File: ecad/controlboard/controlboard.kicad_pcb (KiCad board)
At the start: 2 copper layers, 50 x 100 mm, 39 parts, among them J1 B6B-XH-A(LF)(SN), SW1 KSC_SLT_241G_LFS

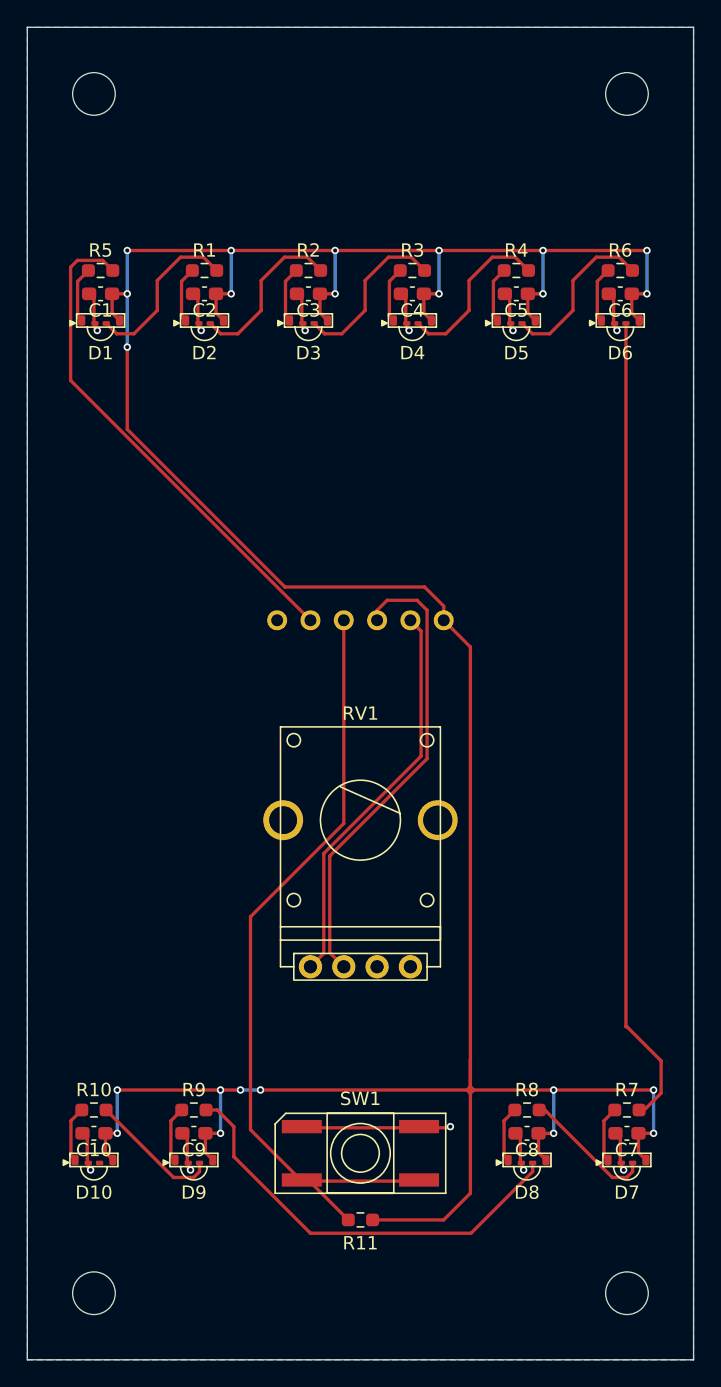
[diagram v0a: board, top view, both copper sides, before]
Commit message: Small changes and cleanup as 3dmodels are pieced together.
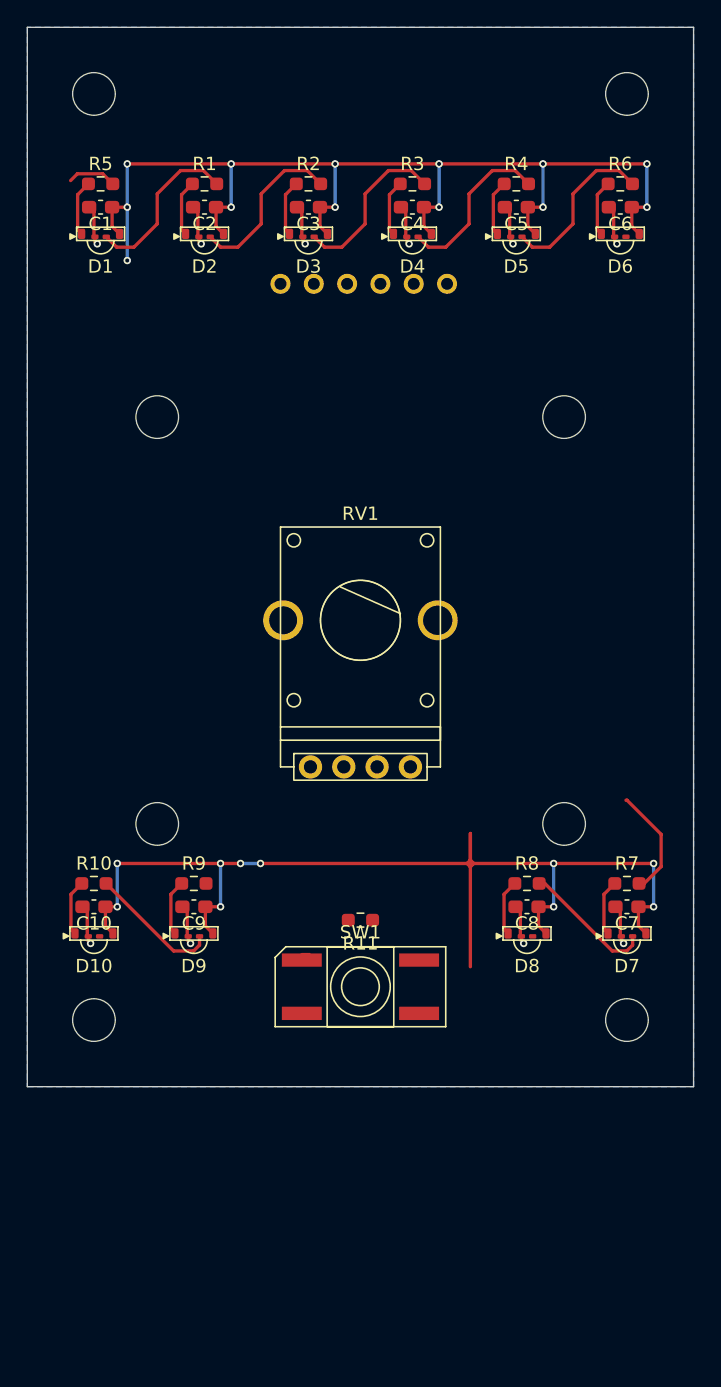
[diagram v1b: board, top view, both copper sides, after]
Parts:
- added REF**: MountingHole_3.2mm_M3, MountingHole:MountingHole_3.2mm_M3, F.Cu at (132.2, 79.8)
- added REF**4: MountingHole_3.2mm_M3, MountingHole:MountingHole_3.2mm_M3, F.Cu at (162.8, 79.8)
- added REF**5: MountingHole_3.2mm_M3, MountingHole:MountingHole_3.2mm_M3, F.Cu at (132.2, 110.3)
- added REF**6: MountingHole_3.2mm_M3, MountingHole:MountingHole_3.2mm_M3, F.Cu at (162.8, 110.3)
- moved J1 25.3 mm to (147.8, 69.8)
- moved R11 22.5 mm to (147.5, 117.5)
- moved REF**2 20.5 mm to (127.5, 125.0)
- moved REF**3 20.5 mm to (167.5, 125.0)
- moved C10 17.0 mm to (127.5, 116.5)
- moved C7 17.0 mm to (167.5, 116.5)
- moved C8 17.0 mm to (160.0, 116.5)
- moved C9 17.0 mm to (135.0, 116.5)
- moved D10 17.0 mm to (127.5, 118.5)
- moved D7 17.0 mm to (167.5, 118.5)
- moved D8 17.0 mm to (160.0, 118.5)
- moved D9 17.0 mm to (135.0, 118.5)
- moved R10 17.0 mm to (127.5, 114.8)
- moved R7 17.0 mm to (167.5, 114.8)
- moved R8 17.0 mm to (160.0, 114.8)
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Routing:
- net +5V: track 240.3 -> 161.9 mm
- net Net-(J1-Pad3): track 60.1 -> 0.00 mm
- net Net-(D6-DOut): track 61.1 -> 8.30 mm
- net Net-(J1-Pad4): track 35.3 -> 0.00 mm
- net Net-(J1-Pad2): track 37.6 -> 3.69 mm
- net Net-(D8-DOut): track 32.2 -> 0.00 mm
- net Net-(J1-Pad5): track 29.8 -> 0.00 mm
- net GND: track 41.2 -> 30.6 mm, vias 11 -> 10
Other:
- board size 50 x 100 mm -> 50 x 79.5 mm

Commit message: Change addressable LED to new part that is still available.
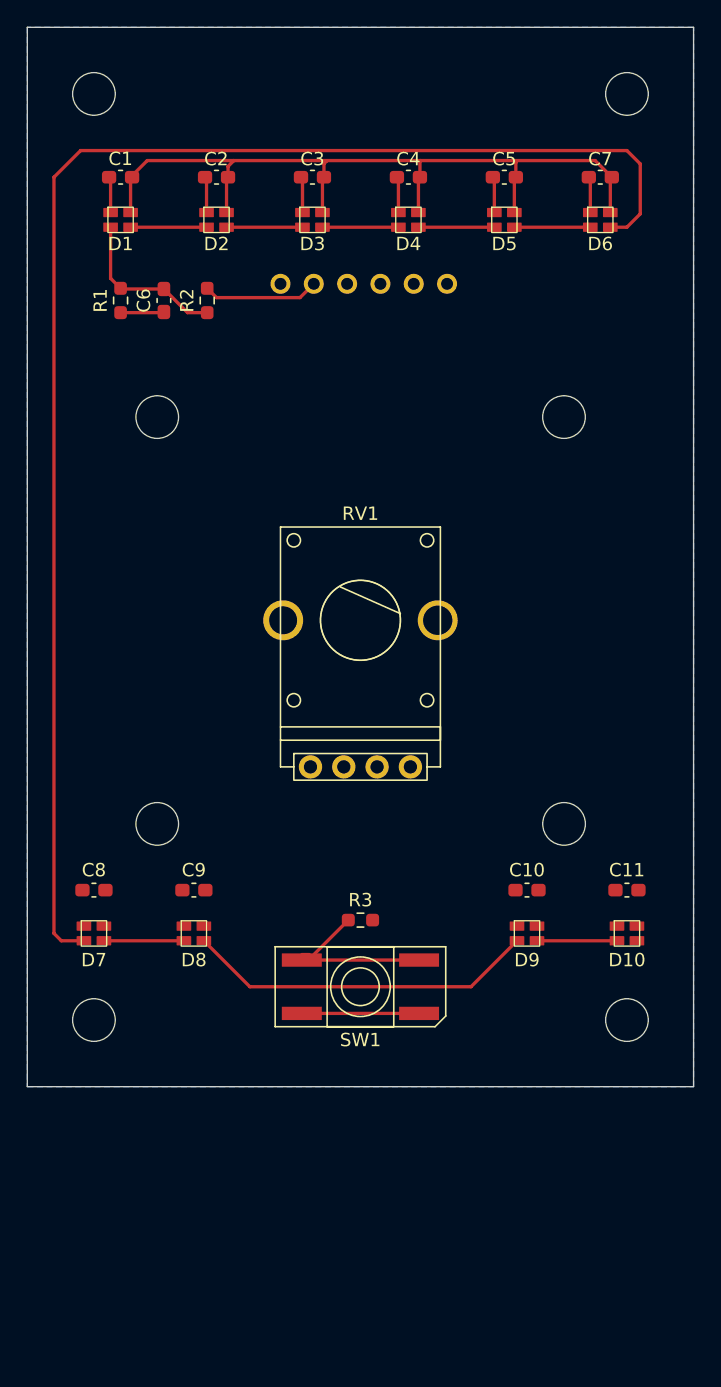
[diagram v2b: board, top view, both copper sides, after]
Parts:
- removed the R1 at (135.8, 62.2)
- removed R10, R4, R6, R7, R8, R9: 33, Resistor_SMD:R_0603_1608Metric_Pad0.98x0.95mm_HandSolder
- removed the R3 at (151.4, 62.2)
- removed REF**1, REF**2, REF**3, REF**4, REF**5, REF**6: MountingHole_3.2mm_M3, MountingHole:MountingHole_3.2mm_M3
- removed control_plate: Board, PCM_kikit:Board
- added C6: 0.1u, Capacitor_SMD:C_0603_1608Metric_Pad1.08x0.95mm_HandSolder, F.Cu at (132.8, 71.0)
- added REF**: MountingHole_3.2mm_M3, MountingHole:MountingHole_3.2mm_M3, F.Cu at (162.8, 110.3)
- added REF**: MountingHole_3.2mm_M3, MountingHole:MountingHole_3.2mm_M3, F.Cu at (167.5, 55.5)
- added REF**: MountingHole_3.2mm_M3, MountingHole:MountingHole_3.2mm_M3, F.Cu at (162.8, 79.8)
- added REF**: MountingHole_3.2mm_M3, MountingHole:MountingHole_3.2mm_M3, F.Cu at (167.5, 125.0)
- added REF**: MountingHole_3.2mm_M3, MountingHole:MountingHole_3.2mm_M3, F.Cu at (132.2, 110.3)
- added REF**: MountingHole_3.2mm_M3, MountingHole:MountingHole_3.2mm_M3, F.Cu at (127.5, 125.0)
- D1, D10, D2, D3, D4, D5, D6, D7, D8, D9: value 12-23C/RSGHBHW-5V01/2C -> 19-C47/RSGHBHC-5V01/2T; footprint silver-box-feetprints:12-23C-RSGHBHW-5V01-2C -> silver-box-feetprints:19-C47 RSGHBHC-5V01 2T
- R1: renamed from R5; value 33 -> 100k
- R2: value 33 -> 10
- moved C11 40.0 mm to (167.5, 115.2)
- moved C8 40.0 mm to (127.5, 115.2)
- moved D10 40.0 mm to (167.5, 118.5)
- moved D7 40.0 mm to (127.5, 118.5)
- moved C10 25.0 mm to (160.0, 115.2)
- moved C9 25.0 mm to (135.0, 115.2)
- moved D8 25.0 mm to (135.0, 118.5)
- moved D9 25.0 mm to (160.0, 118.5)
- moved R2 11.6 mm to (136.0, 71.0), turned to 90 degrees
- moved R1 8.88 mm to (129.5, 71.0), turned to 90 degrees
- moved C1 2.70 mm to (129.5, 61.8)
- moved C7 2.70 mm to (165.5, 61.8)
- moved C2 2.42 mm to (136.7, 61.8)
- moved C5 2.42 mm to (158.3, 61.8)
- moved C3 2.27 mm to (143.9, 61.8)
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- renumbered C9 to C10, C10 to C11, C6 to C7, C7 to C8, C8 to C9, R11 to R3
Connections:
- D1 pad 1: Net-(D1-DIn) -> Net-(D1-DOut)
- D1 pad 2: GND -> +5V
- D1 pad 3: Net-(D1-DOut) -> Net-(D1-DIn)
- D1 pad 4: +5V -> GND
- D10 pad 1: Net-(D10-DIn) -> unconnected-(D10-DOut-Pad1)
- D10 pad 2: GND -> +5V
- D10 pad 3: unconnected-(D10-DOut-Pad3) -> Net-(D10-DIn)
- D10 pad 4: +5V -> GND
- D2 pad 1: Net-(D2-DIn) -> Net-(D2-DOut)
- D2 pad 2: GND -> +5V
- D2 pad 3: Net-(D2-DOut) -> Net-(D1-DOut)
- D2 pad 4: +5V -> GND
- D3 pad 1: Net-(D3-DIn) -> Net-(D3-DOut)
- D3 pad 2: GND -> +5V
- D3 pad 3: Net-(D3-DOut) -> Net-(D2-DOut)
- D3 pad 4: +5V -> GND
- D4 pad 1: Net-(D4-DIn) -> Net-(D4-DOut)
- D4 pad 2: GND -> +5V
- D4 pad 3: Net-(D4-DOut) -> Net-(D3-DOut)
- D4 pad 4: +5V -> GND
- D5 pad 1: Net-(D5-DIn) -> Net-(D5-DOut)
- D5 pad 2: GND -> +5V
- D5 pad 3: Net-(D5-DOut) -> Net-(D4-DOut)
- D5 pad 4: +5V -> GND
- D6 pad 1: Net-(D6-DIn) -> Net-(D6-DOut)
- D6 pad 2: GND -> +5V
- D6 pad 3: Net-(D6-DOut) -> Net-(D5-DOut)
- D6 pad 4: +5V -> GND
- D7 pad 1: Net-(D7-DIn) -> Net-(D7-DOut)
- D7 pad 2: GND -> +5V
- D7 pad 3: Net-(D7-DOut) -> Net-(D6-DOut)
- D7 pad 4: +5V -> GND
- D8 pad 1: Net-(D8-DIn) -> Net-(D8-DOut)
- D8 pad 2: GND -> +5V
- D8 pad 3: Net-(D8-DOut) -> Net-(D7-DOut)
- D8 pad 4: +5V -> GND
- D9 pad 1: Net-(D9-DIn) -> Net-(D10-DIn)
- D9 pad 2: GND -> +5V
- D9 pad 3: Net-(D9-DOut) -> Net-(D8-DOut)
- D9 pad 4: +5V -> GND
- R1 pad 1: Net-(D1-DIn) -> GND
- R1 pad 2: Net-(J1-Pad2) -> Net-(D1-DIn)
- R2 pad 1: Net-(D3-DIn) -> Net-(D1-DIn)
- R2 pad 2: Net-(D2-DOut) -> Net-(J1-Pad2)
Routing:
- net +5V: track 161.9 -> 58.6 mm, vias 23 -> 0
- net Net-(D6-DOut): track 8.30 -> 110.9 mm
- net Net-(D8-DOut): track 0.00 -> 26.4 mm
- net Net-(J1-Pad3): track 0.00 -> 14.1 mm
- net Net-(D9-DOut): track 9.95 -> 0.00 mm
- net Net-(D1-DIn): track 4.21 -> 12.2 mm
- net Net-(D3-DOut): track 12.7 -> 5.70 mm
- net Net-(D5-DOut): track 12.7 -> 5.70 mm
- net Net-(D4-DOut): track 12.7 -> 5.70 mm
- net Net-(D1-DOut): track 12.7 -> 5.70 mm
- net Net-(D2-DOut): track 12.7 -> 5.70 mm
- net Net-(J1-Pad2): track 3.69 -> 8.72 mm
- net Net-(D5-DIn): track 4.21 -> 0.00 mm
- net Net-(D3-DIn): track 4.21 -> 0.00 mm
- net Net-(D2-DIn): track 4.21 -> 0.00 mm
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
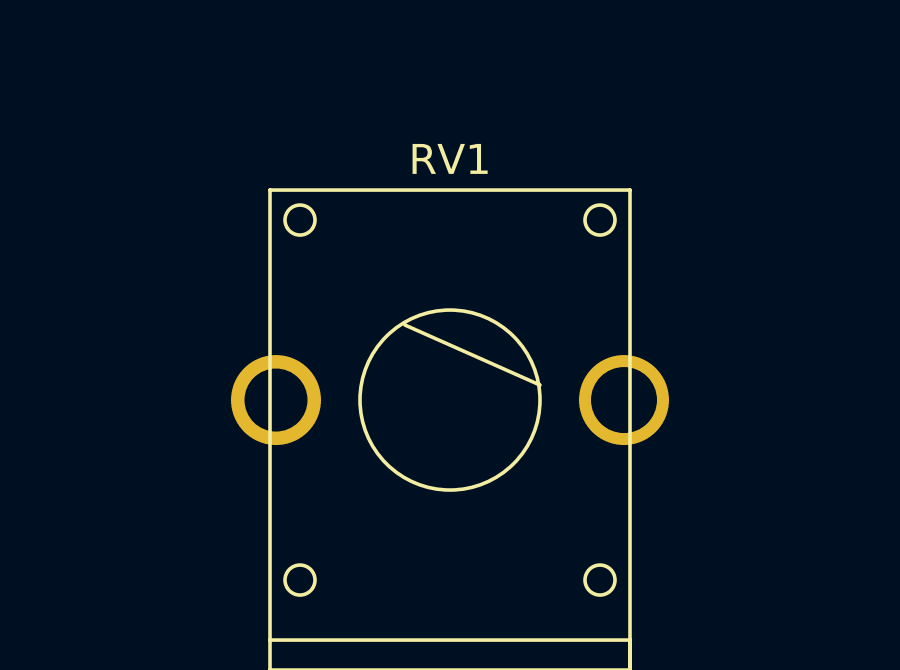
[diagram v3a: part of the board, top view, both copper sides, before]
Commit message: Fix 3d models getting duplicated output in .step export
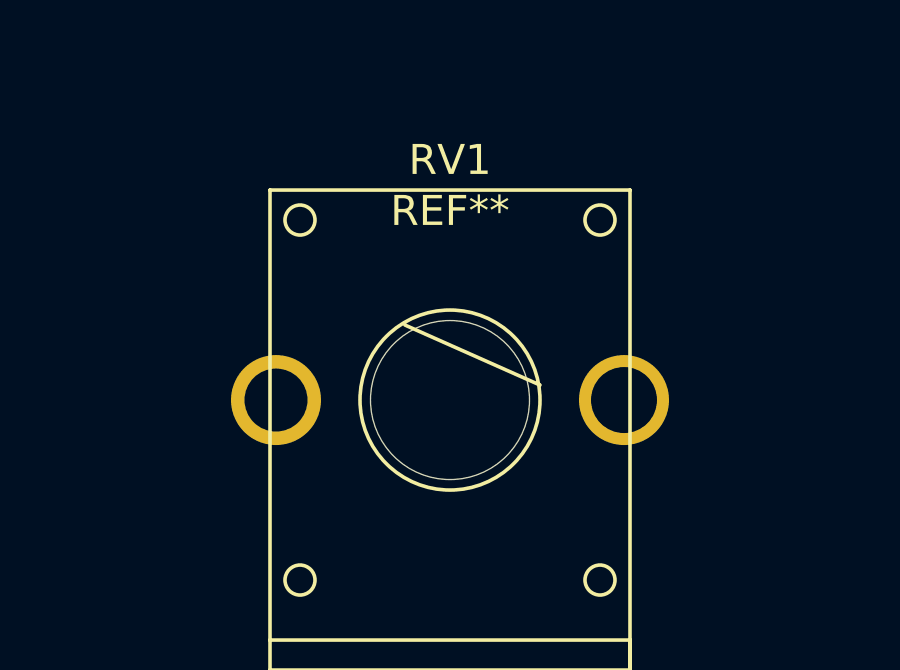
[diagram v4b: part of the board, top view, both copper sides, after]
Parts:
- added REF**: MountingHole_5.3mm_M5, MountingHole:MountingHole_5.3mm_M5, F.Cu at (147.5, 95.0)
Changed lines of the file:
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@@
-      (rotate (xyz 0 0 0))
-    )
-    (model "../../mcad/19-C47 RSGHBHC-5V01 2T.wrl"
-      (offset (xyz 0 0 0))
-      (scale (xyz 0.394 0.394 0.394))
       (rotate (xyz 0 0 0))
     )
@@
       (rotate (xyz 0 0 0))
     )
-    (model "../../mcad/19-C47 RSGHBHC-5V01 2T.wrl"
-      (offset (xyz 0 0 0))
-      (scale (xyz 0.394 0.394 0.394))
-      (rotate (xyz 0 0 0))
-    )
   )
   (footprint "Capacitor_SMD:C_0603_1608Metric_Pad1.08x0.95mm_HandSolder" (layer "F.Cu")
@@
       (rotate (xyz 0 0 0))
     )
-    (model "../../mcad/19-C47 RSGHBHC-5V01 2T.wrl"
-      (offset (xyz 0 0 0))
-      (scale (xyz 0.394 0.394 0.394))
-      (rotate (xyz 0 0 0))
-    )
   )
   (footprint "Capacitor_SMD:C_0603_1608Metric_Pad1.08x0.95mm_HandSolder" (layer "F.Cu")
@@
       (rotate (xyz 0 0 0))
     )
-    (model "../../mcad/19-C47 RSGHBHC-5V01 2T.wrl"
-      (offset (xyz 0 0 0))
-      (scale (xyz 0.394 0.394 0.394))
-      (rotate (xyz 0 0 0))
-    )
   )
   (footprint "silver-box-feetprints:19-C47 RSGHBHC-5V01 2T" (layer "F.Cu")
@@
       (rotate (xyz 0 0 0))
     )
-    (model "../../mcad/19-C47 RSGHBHC-5V01 2T.wrl"
-      (offset (xyz 0 0 0))
-      (scale (xyz 0.394 0.394 0.394))
-      (rotate (xyz 0 0 0))
-    )
   )
   (footprint "Resistor_SMD:R_0603_1608Metric_Pad0.98x0.95mm_HandSolder" (layer "F.Cu")
@@
       (rotate (xyz 0 0 0))
     )
-    (model "../../mcad/19-C47 RSGHBHC-5V01 2T.wrl"
-      (offset (xyz 0 0 0))
-      (scale (xyz 0.394 0.394 0.394))
-      (rotate (xyz 0 0 0))
-    )
   )
   (footprint "Capacitor_SMD:C_0603_1608Metric_Pad1.08x0.95mm_HandSolder" (layer "F.Cu")
@@
       (rotate (xyz 0 0 0))
     )
-    (model "../../mcad/19-C47 RSGHBHC-5V01 2T.wrl"
-      (offset (xyz 0 0 0))
-      (scale (xyz 0.394 0.394 0.394))
-      (rotate (xyz 0 0 0))
-    )
   )
   (footprint "silver-box-feetprints:19-C47 RSGHBHC-5V01 2T" (layer "F.Cu")
@@
       (rotate (xyz 0 0 0))
     )
-    (model "../../mcad/19-C47 RSGHBHC-5V01 2T.wrl"
-      (offset (xyz 0 0 0))
-      (scale (xyz 0.394 0.394 0.394))
-      (rotate (xyz 0 0 0))
-    )
   )
   (footprint "Capacitor_SMD:C_0603_1608Metric_Pad1.08x0.95mm_HandSolder" (layer "F.Cu")
@@
       (rotate (xyz 0 0 0))
     )
+  )
+  (footprint "MountingHole:MountingHole_5.3mm_M5" (layer "F.Cu")
+    (at 147.5 95)
+    (descr "Mounting Hole 5.3mm, no annular, M5")
+    (tags "mounting hole 5.3mm no annular m5")
+    (attr exclude_from_pos_files exclude_from_bom)
+    (fp_text reference "REF**" (at 0 -6.3) (layer "F.SilkS")
+        (effects (font (size 1 1) (thickness 0.15)))
+    )
+    (fp_text value "MountingHole_5.3mm_M5" (at 0 6.3) (layer "F.Fab")
+        (effects (font (size 1 1) (thickness 0.15)))
+    )
+    (fp_text user "${REFERENCE}" (at 0 0) (layer "F.Fab")
+        (effects (font (size 1 1) (thickness 0.15)))
+    )
+    (fp_circle (center 0 0) (end 5.3 0)
+      (stroke (width 0.15) (type solid)) (fill none) (layer "Cmts.User"))
+    (fp_circle (center 0 0) (end 5.55 0)
+      (stroke (width 0.05) (type solid)) (fill none) (layer "F.CrtYd"))
+    (pad "" np_thru_hole circle (at 0 0) (size 5.3 5.3) (drill 5.3) (layers "*.Cu" "*.Mask"))
   )
   (footprint "Resistor_SMD:R_0603_1608Metric_Pad0.98x0.95mm_HandSolder" (layer "F.Cu")
@@
     (pad "4" smd rect (at -4.4 -2 90) (size 1 3) (layers "F.Cu" "F.Paste" "F.Mask")
       (net 16 "GND") (pintype "passive"))
-    (model "C:/Users/boxca/Google Drive/Projects/silver-box-modular/mcad/CK switches KSC SLT G.step"
-      (offset (xyz 0 0 0))
-      (scale (xyz 1 1 1))
-      (rotate (xyz 0 0 90))
-    )
-    (model "C:/Users/boxca/Google Drive/Projects/silver-box-modular/mcad/CK switches KSC SLT G.wrl"
-      (offset (xyz 0 0 0))
-      (scale (xyz 0.394 0.394 0.394))
+    (model "../../mcad/CK switches KSC SLT G.step"
+      (offset (xyz 0 0 0))
+      (scale (xyz 1 1 1))
       (rotate (xyz 0 0 90))
     )
@@
       (offset (xyz 0 0 0))
       (scale (xyz 1 1 1))
-      (rotate (xyz 0 0 0))
-    )
-    (model "../../mcad/19-C47 RSGHBHC-5V01 2T.wrl"
-      (offset (xyz 0 0 0))
-      (scale (xyz 0.394 0.394 0.394))
       (rotate (xyz 0 0 0))
     )
@@
     (fp_rect (start 7.5 12.5) (end -7.5 -7.5)
       (stroke (width 0.05) (type solid)) (fill none) (layer "F.CrtYd"))
-    (pad "" np_thru_hole circle (at -5.8 0) (size 3 3) (drill 2.1) (layers "*.Cu" "*.Mask"))
-    (pad "" np_thru_hole circle (at 0 0) (size 1.524 1.524) (drill 6) (layers "*.Mask"))
-    (pad "" np_thru_hole circle (at 3.75 11) (size 1.75 1.75) (drill 1) (layers "*.Cu" "*.Mask"))
-    (pad "" np_thru_hole circle (at 5.8 0) (size 3 3) (drill 2.2) (layers "*.Cu" "*.Mask"))
+    (pad "" np_thru_hole circle (at -5.8 0) (size 3 3) (drill 2.1) (layers "F&B.Cu" "*.Mask"))
+    (pad "" np_thru_hole circle (at 3.75 11) (size 1.75 1.75) (drill 1) (layers "F&B.Cu" "*.Mask"))
+    (pad "" np_thru_hole circle (at 5.8 0) (size 3 3) (drill 2.2) (layers "F&B.Cu" "*.Mask"))
     (pad "1" thru_hole circle (at -3.75 11) (size 1.75 1.75) (drill 1) (layers "*.Cu" "*.Mask")
       (net 14 "Net-(J1-Pad5)") (pinfunction "1") (pintype "passive"))
@@
     (pad "3" thru_hole circle (at 1.25 11) (size 1.75 1.75) (drill 1) (layers "*.Cu" "*.Mask")
       (net 16 "GND") (pinfunction "3") (pintype "passive"))
-    (model "C:/Users/boxca/Google Drive/Projects/silver-box-modular/mcad/bourns PTV111-4425A.step"
-      (offset (xyz 0 0 0))
-      (scale (xyz 1 1 1))
-      (rotate (xyz 0 0 0))
-    )
-    (model "C:/Users/boxca/Google Drive/Projects/silver-box-modular/mcad/bourns PTV111-4425A.wrl"
-      (offset (xyz 0 0 0))
-      (scale (xyz 0.394 0.394 0.394))
+    (model "../../mcad/bourns PTV111-4425A.step"
+      (offset (xyz 0 0 0))
+      (scale (xyz 1 1 1))
       (rotate (xyz 0 0 0))
     )
@@
       (offset (xyz 0 0 0))
       (scale (xyz 1 1 1))
-      (rotate (xyz 0 0 0))
-    )
-    (model "../../mcad/19-C47 RSGHBHC-5V01 2T.wrl"
-      (offset (xyz 0 0 0))
-      (scale (xyz 0.394 0.394 0.394))
       (rotate (xyz 0 0 0))
     )
@@
       (offset (xyz 0 0 0))
       (scale (xyz 1 1 1))
-      (rotate (xyz 0 0 0))
-    )
-    (model "../../mcad/jst-xh-6a.wrl" hide
-      (offset (xyz 0 0 0))
-      (scale (xyz 1 1 1))
